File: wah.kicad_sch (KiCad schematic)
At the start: 20 parts, among them Q7 2N3904, Q8 2N3904

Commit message: Actualización de esquemáticos
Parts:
- R31, R32, R33, R34, R35, R36, R37, R38, R39, R40, R41: footprint (none) -> Resistor_THT:R_Axial_DIN0207_L6.3mm_D2.5mm_P7.62mm_Horizontal
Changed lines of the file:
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@@
 (kicad_sch
-	(version 20231120)
+	(version 20250114)
 	(generator "eeschema")
-	(generator_version "8.0")
+	(generator_version "9.0")
 	(paper "A4")
 	(junction
@@
 			)
 		)
-		(property "Footprint" ""
+		(property "Footprint" "Resistor_THT:R_Axial_DIN0207_L6.3mm_D2.5mm_P7.62mm_Horizontal"
 			(at 146.812 81.28 90)
 			(effects
@@
 			)
 		)
-		(property "Footprint" ""
+		(property "Footprint" "Resistor_THT:R_Axial_DIN0207_L6.3mm_D2.5mm_P7.62mm_Horizontal"
 			(at 115.062 88.9 90)
 			(effects
@@
 			)
 		)
-		(property "Footprint" ""
+		(property "Footprint" "Resistor_THT:R_Axial_DIN0207_L6.3mm_D2.5mm_P7.62mm_Horizontal"
 			(at 146.812 119.38 90)
 			(effects
@@
 			)
 		)
-		(property "Footprint" ""
+		(property "Footprint" "Resistor_THT:R_Axial_DIN0207_L6.3mm_D2.5mm_P7.62mm_Horizontal"
 			(at 125.73 135.128 90)
 			(effects
@@
 			)
 		)
-		(property "Footprint" ""
+		(property "Footprint" "Resistor_THT:R_Axial_DIN0207_L6.3mm_D2.5mm_P7.62mm_Horizontal"
 			(at 160.782 81.28 90)
 			(effects
@@
 			)
 		)
-		(property "Footprint" ""
+		(property "Footprint" "Resistor_THT:R_Axial_DIN0207_L6.3mm_D2.5mm_P7.62mm_Horizontal"
 			(at 105.918 88.9 90)
 			(effects
@@
 			)
 		)
-		(property "Footprint" ""
+		(property "Footprint" "Resistor_THT:R_Axial_DIN0207_L6.3mm_D2.5mm_P7.62mm_Horizontal"
 			(at 115.062 55.88 90)
 			(effects
@@
 			)
 		)
-		(property "Footprint" ""
+		(property "Footprint" "Resistor_THT:R_Axial_DIN0207_L6.3mm_D2.5mm_P7.62mm_Horizontal"
 			(at 88.392 120.65 90)
 			(effects
@@
 			)
 		)
-		(property "Footprint" ""
+		(property "Footprint" "Resistor_THT:R_Axial_DIN0207_L6.3mm_D2.5mm_P7.62mm_Horizontal"
 			(at 102.362 144.78 90)
 			(effects
@@
 			)
 		)
-		(property "Footprint" ""
+		(property "Footprint" "Resistor_THT:R_Axial_DIN0207_L6.3mm_D2.5mm_P7.62mm_Horizontal"
 			(at 75.692 86.36 90)
 			(effects
@@
 			)
 		)
-		(property "Footprint" ""
+		(property "Footprint" "Resistor_THT:R_Axial_DIN0207_L6.3mm_D2.5mm_P7.62mm_Horizontal"
 			(at 95.25 80.518 90)
 			(effects

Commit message: Actualización esquemáticos
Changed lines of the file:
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@@
+	(wire
+		(pts
+			(xy 129.54 133.35) (xy 228.6 133.35)
+		)
+		(stroke
+			(width 0)
+			(type default)
+		)
+	)
 	(wire
 		(pts
@@
 	(wire
 		(pts
-			(xy 129.54 133.35) (xy 207.01 133.35)
-		)
-		(stroke
-			(width 0)
-			(type default)
-		)
-	)
-	(wire
-		(pts
 			(xy 116.84 92.71) (xy 116.84 93.98)
 		)
@@
 	(wire
 		(pts
-			(xy 207.01 49.53) (xy 207.01 133.35)
+			(xy 228.6 50.8) (xy 228.6 133.35)
 		)
 		(stroke
@@
 	(wire
 		(pts
-			(xy 207.01 49.53) (xy 162.56 49.53)
+			(xy 228.6 50.8) (xy 162.56 50.8)
 		)
 		(stroke
@@
 	(wire
 		(pts
-			(xy 162.56 49.53) (xy 162.56 66.04)
+			(xy 162.56 50.8) (xy 162.56 66.04)
 		)
 		(stroke
@@
 			)
 		)
-		(property "Description" ""
+		(property "Description" "Power symbol creates a global label with name \"VCC\""
 			(at 148.59 76.2 0)
 			(effects
@@
 	)
 	(symbol
+		(lib_name "GND_1")
 		(lib_id "power:GND")
 		(at 77.47 91.44 0)
@@
 			)
 		)
-		(property "Description" ""
+		(property "Description" "Power symbol creates a global label with name \"GND\" , ground"
 			(at 77.47 91.44 0)
 			(effects
@@
 			)
 		)
-		(property "Description" ""
+		(property "Description" "Power symbol creates a global label with name \"GND\" , ground"
 			(at 186.69 101.6 0)
 			(effects
@@
 			)
 		)
-		(property "Description" ""
+		(property "Description" "0.2A Ic, 40V Vce, Small Signal NPN Transistor, TO-92"
 			(at 151.13 96.52 0)
 			(effects
@@
 	)
 	(symbol
+		(lib_name "GND_2")
 		(lib_id "power:GND")
 		(at 116.84 93.98 0)
@@
 			)
 		)
-		(property "Description" ""
+		(property "Description" "Power symbol creates a global label with name \"GND\" , ground"
 			(at 116.84 93.98 0)
 			(effects
@@
 	)
 	(symbol
+		(lib_name "GND_4")
 		(lib_id "power:GND")
 		(at 104.14 158.75 0)
@@
 			)
 		)
-		(property "Description" ""
+		(property "Description" "Power symbol creates a global label with name \"GND\" , ground"
 			(at 104.14 158.75 0)
 			(effects
@@
 	)
 	(symbol
+		(lib_name "GND_3")
 		(lib_id "power:GND")
 		(at 148.59 124.46 0)
@@
 			)
 		)
-		(property "Description" ""
+		(property "Description" "Power symbol creates a global label with name \"GND\" , ground"
 			(at 148.59 124.46 0)
 			(effects
@@
 			)
 		)
-		(property "Description" ""
+		(property "Description" "Power symbol creates a global label with name \"VCC\""
 			(at 116.84 50.8 0)
 			(effects
@@
 	)
 	(symbol
+		(lib_name "2N3904_1")
 		(lib_id "Transistor_BJT:2N3904")
 		(at 114.3 78.74 0)
@@
 			)
 		)
-		(property "Description" ""
+		(property "Description" "0.2A Ic, 40V Vce, Small Signal NPN Transistor, TO-92"
 			(at 114.3 78.74 0)
 			(effects

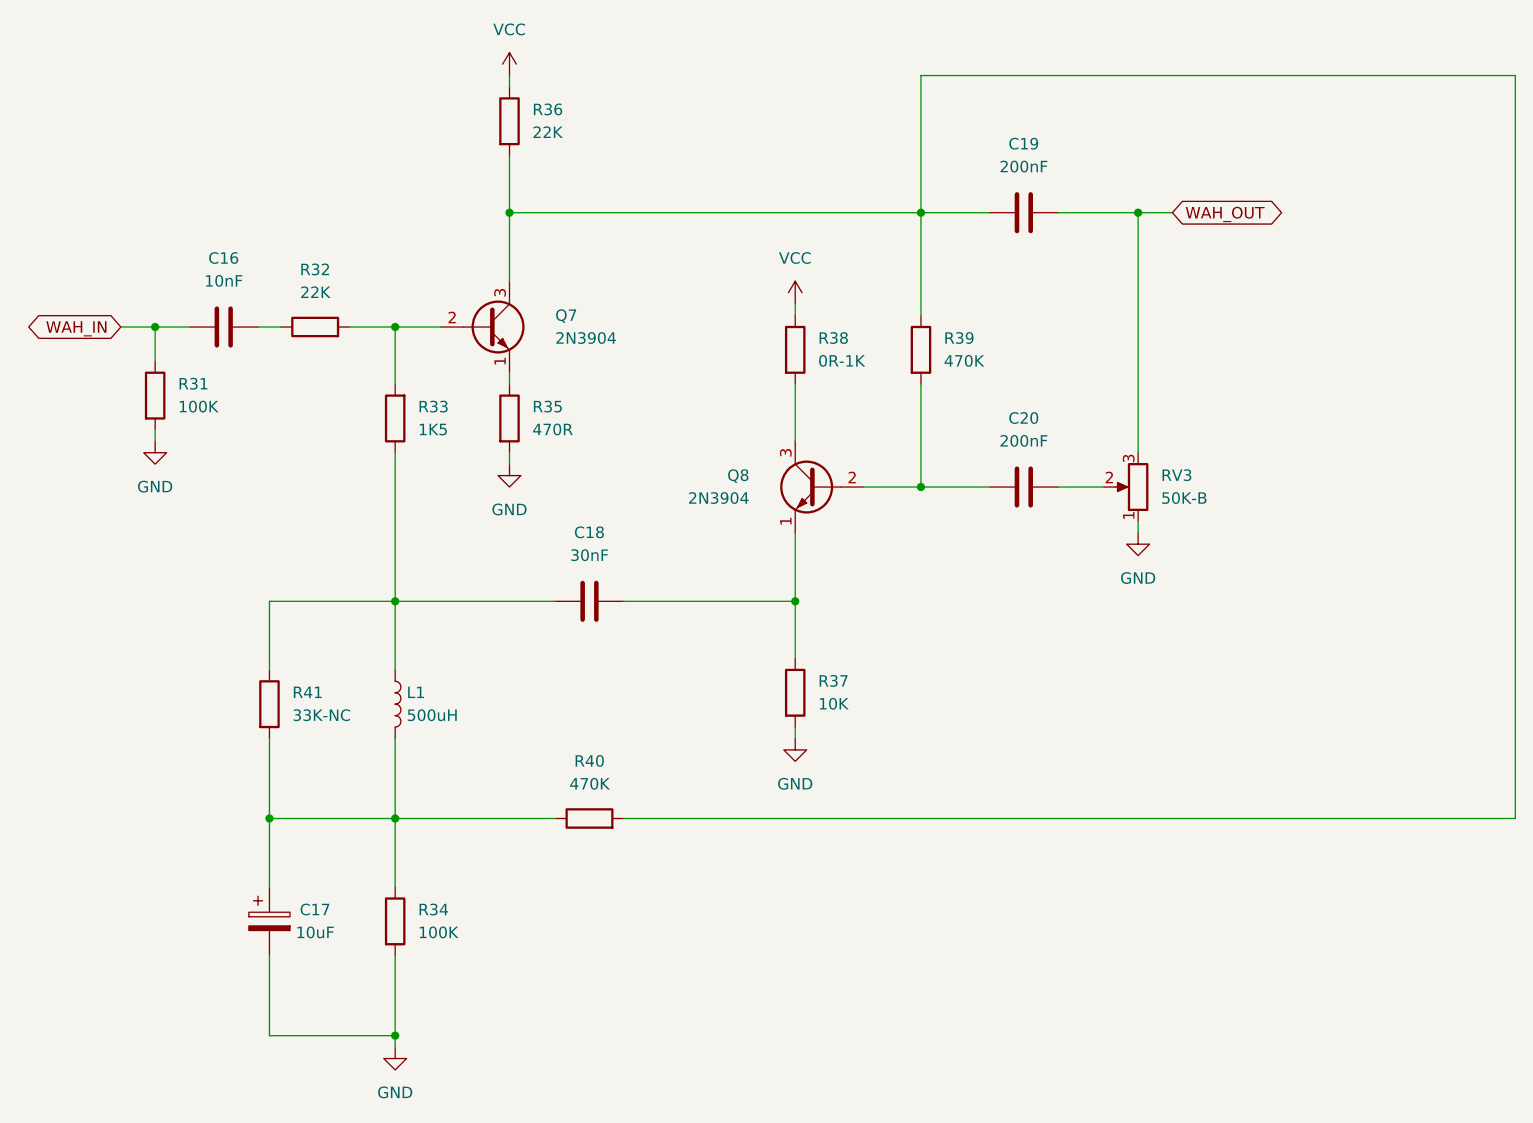
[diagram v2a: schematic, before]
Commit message: Asignación de huellas a componentes.
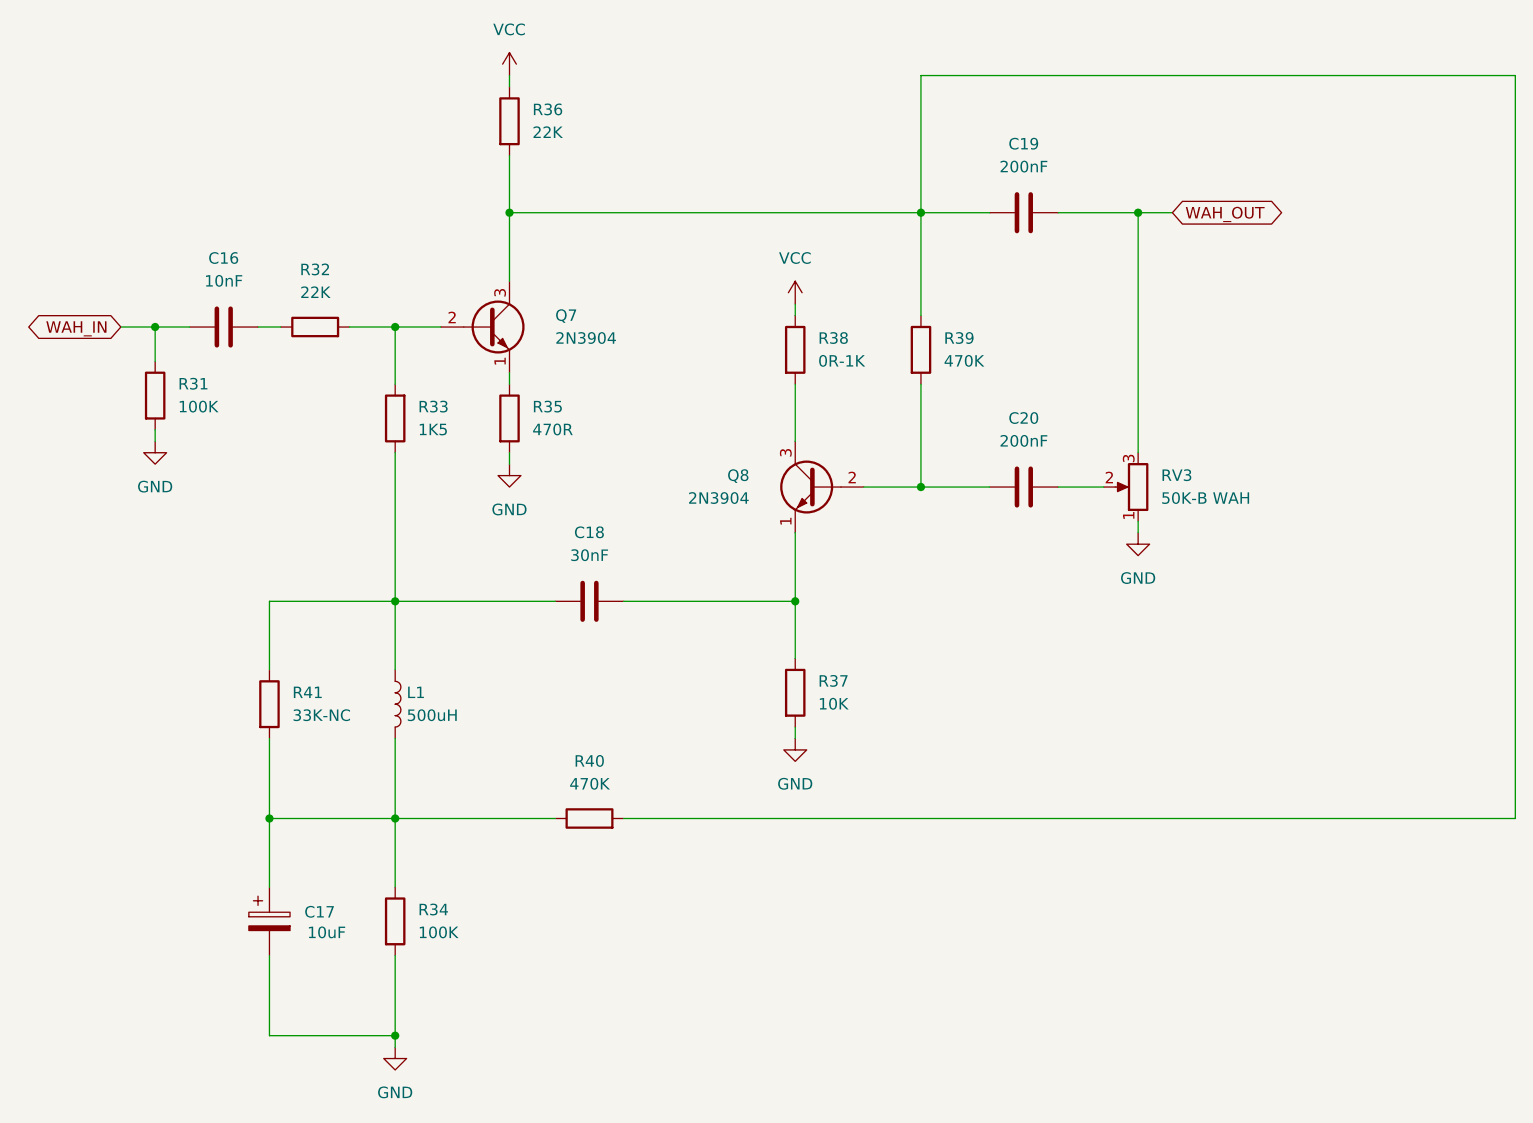
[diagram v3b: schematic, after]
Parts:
- C16, C18, C19, C20: footprint (none) -> Capacitor_THT:C_Disc_D5.1mm_W3.2mm_P5.00mm
- C17: footprint (none) -> Capacitor_THT:CP_Radial_D5.0mm_P2.00mm
- L1: footprint (none) -> Inductor_THT:L_Radial_D16.8mm_P11.43mm_Vishay_IHB-1
- RV3: value 50K-B -> 50K-B WAH; footprint (none) -> DIY_jorge:Pot Alpha 16mm
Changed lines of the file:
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@@
 			)
 		)
-		(property "Footprint" ""
+		(property "Footprint" "Capacitor_THT:C_Disc_D5.1mm_W3.2mm_P5.00mm"
 			(at 88.9 77.7748 0)
 			(effects
@@
 	)
 	(symbol
-		(lib_id "Device:C_Polarized")
-		(at 90.17 144.78 0)
-		(unit 1)
-		(exclude_from_sim no)
-		(in_bom yes)
-		(on_board yes)
-		(dnp no)
-		(property "Reference" "C17"
-			(at 95.25 143.51 0)
-			(effects
-				(font
-					(size 1.27 1.27)
-				)
-			)
-		)
-		(property "Value" "10uF"
-			(at 95.25 146.05 0)
-			(effects
-				(font
-					(size 1.27 1.27)
-				)
-			)
-		)
-		(property "Footprint" ""
-			(at 91.1352 148.59 0)
-			(effects
-				(font
-					(size 1.27 1.27)
-				)
-				(hide yes)
-			)
-		)
-		(property "Datasheet" "~"
-			(at 90.17 144.78 0)
-			(effects
-				(font
-					(size 1.27 1.27)
-				)
-				(hide yes)
-			)
-		)
-		(property "Description" ""
-			(at 90.17 144.78 0)
-			(effects
-				(font
-					(size 1.27 1.27)
-				)
-				(hide yes)
-			)
-		)
-		(pin "1"
-		)
-		(pin "2"
-		)
-		(instances
-			(project "test"
-				(path "/6df9a4de-ce35-4607-9a42-d3c459c15494/072d3036-f4e0-4f4e-8725-744b6c55964f"
-					(reference "C17")
-					(unit 1)
-				)
-			)
-		)
-	)
-	(symbol
 		(lib_name "GND_1")
 		(lib_id "power:GND")
@@
 			)
 		)
-		(property "Footprint" ""
+		(property "Footprint" "Inductor_THT:L_Radial_D16.8mm_P11.43mm_Vishay_IHB-1"
 			(at 104.14 120.65 0)
 			(effects
@@
 			)
 		)
-		(property "Footprint" ""
+		(property "Footprint" "Capacitor_THT:C_Disc_D5.1mm_W3.2mm_P5.00mm"
 			(at 177.8 65.0748 0)
 			(effects
@@
 			)
 		)
-		(property "Footprint" ""
+		(property "Footprint" "Capacitor_THT:C_Disc_D5.1mm_W3.2mm_P5.00mm"
 			(at 177.8 95.5548 0)
 			(effects
@@
 			)
 		)
-		(property "Value" "50K-B"
+		(property "Value" "50K-B WAH"
 			(at 189.23 97.79 0)
 			(effects
@@
 			)
 		)
-		(property "Footprint" ""
+		(property "Footprint" "DIY_jorge:Pot Alpha 16mm"
 			(at 186.69 96.52 0)
 			(effects
@@
 			)
 		)
-		(property "Footprint" ""
+		(property "Footprint" "Capacitor_THT:C_Disc_D5.1mm_W3.2mm_P5.00mm"
 			(at 129.54 108.2548 0)
 			(effects
@@
 					(unit 1)
 				)
+			)
+		)
+	)
+	(symbol
+		(lib_id "Device:C_Polarized")
+		(at 90.17 144.78 0)
+		(unit 1)
+		(exclude_from_sim no)
+		(in_bom yes)
+		(on_board yes)
+		(dnp no)
+		(property "Reference" "C17"
+			(at 95.758 143.764 0)
+			(effects
+				(font
+					(size 1.27 1.27)
+				)
+			)
+		)
+		(property "Value" "10uF"
+			(at 96.52 146.05 0)
+			(effects
+				(font
+					(size 1.27 1.27)
+				)
+			)
+		)
+		(property "Footprint" "Capacitor_THT:CP_Radial_D5.0mm_P2.00mm"
+			(at 91.1352 148.59 0)
+			(effects
+				(font
+					(size 1.27 1.27)
+				)
+				(hide yes)
+			)
+		)
+		(property "Datasheet" "~"
+			(at 90.17 144.78 0)
+			(effects
+				(font
+					(size 1.27 1.27)
+				)
+				(hide yes)
+			)
+		)
+		(property "Description" ""
+			(at 90.17 144.78 0)
+			(effects
+				(font
+					(size 1.27 1.27)
+				)
+				(hide yes)
+			)
+		)
+		(pin "1"
+		)
+		(pin "2"
+		)
+		(instances
+			(project "FuzzWah"
+				(path "/6df9a4de-ce35-4607-9a42-d3c459c15494/072d3036-f4e0-4f4e-8725-744b6c55964f"
+					(reference "C17")
+					(unit 1)
+				)

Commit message: Finalización de PCB (archivos fabricación pendientes)
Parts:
- L1: footprint Inductor_THT:L_Radial_D16.8mm_P11.43mm_Vishay_IHB-1 -> Inductor_THT:L_Radial_D7.2mm_P3.00mm_Murata_1700
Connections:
- net WAH_OUT: now also C19.1; no longer C19.2
- net at Q7.3 (C), R36.2, R39.1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: now also C19.2; no longer C19.1
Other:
- moved on the sheet: C19
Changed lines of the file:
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@@
 			)
 		)
-		(property "Footprint" "Inductor_THT:L_Radial_D16.8mm_P11.43mm_Vishay_IHB-1"
+		(property "Footprint" "Inductor_THT:L_Radial_D7.2mm_P3.00mm_Murata_1700"
 			(at 104.14 120.65 0)
 			(effects
@@
 	(symbol
 		(lib_id "Device:C")
-		(at 173.99 66.04 90)
-		(unit 1)
-		(exclude_from_sim no)
-		(in_bom yes)
-		(on_board yes)
-		(dnp no)
-		(fields_autoplaced yes)
+		(at 173.99 66.04 270)
+		(mirror x)
+		(unit 1)
+		(exclude_from_sim no)
+		(in_bom yes)
+		(on_board yes)
+		(dnp no)
 		(property "Reference" "C19"
 			(at 173.99 58.42 90)
@@
 		)
 		(property "Footprint" "Capacitor_THT:C_Disc_D5.1mm_W3.2mm_P5.00mm"
-			(at 177.8 65.0748 0)
-			(effects
-				(font
+			(at 170.18 65.0748 0)
+			(effects
+				(font
